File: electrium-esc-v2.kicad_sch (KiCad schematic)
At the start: 5 parts, among them J1 CAN

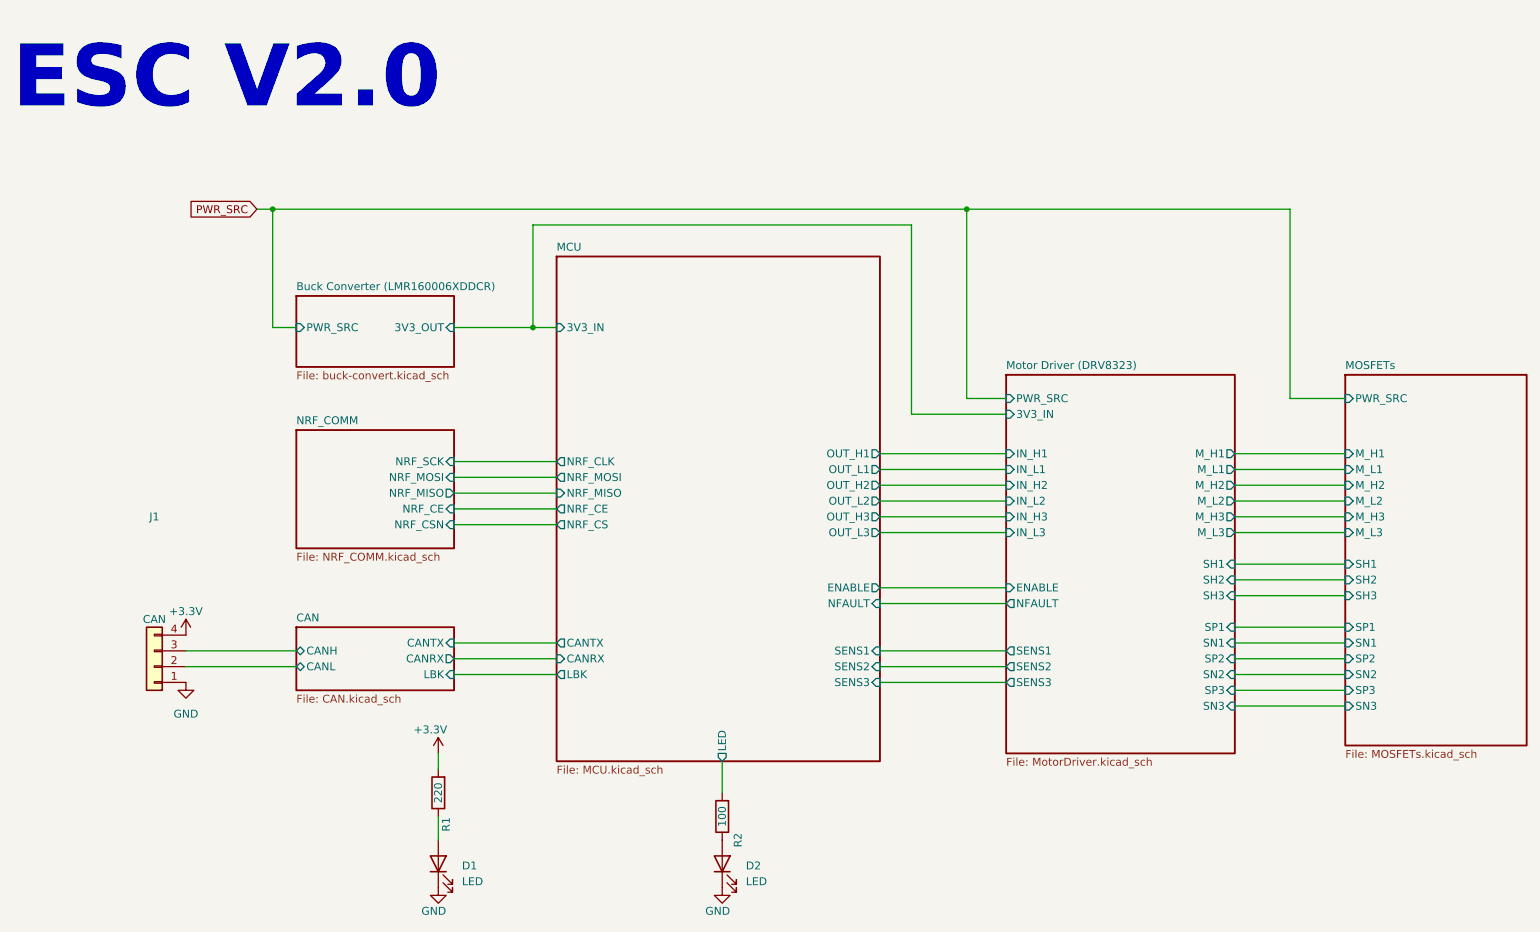
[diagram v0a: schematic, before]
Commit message: Add proper JST Connector
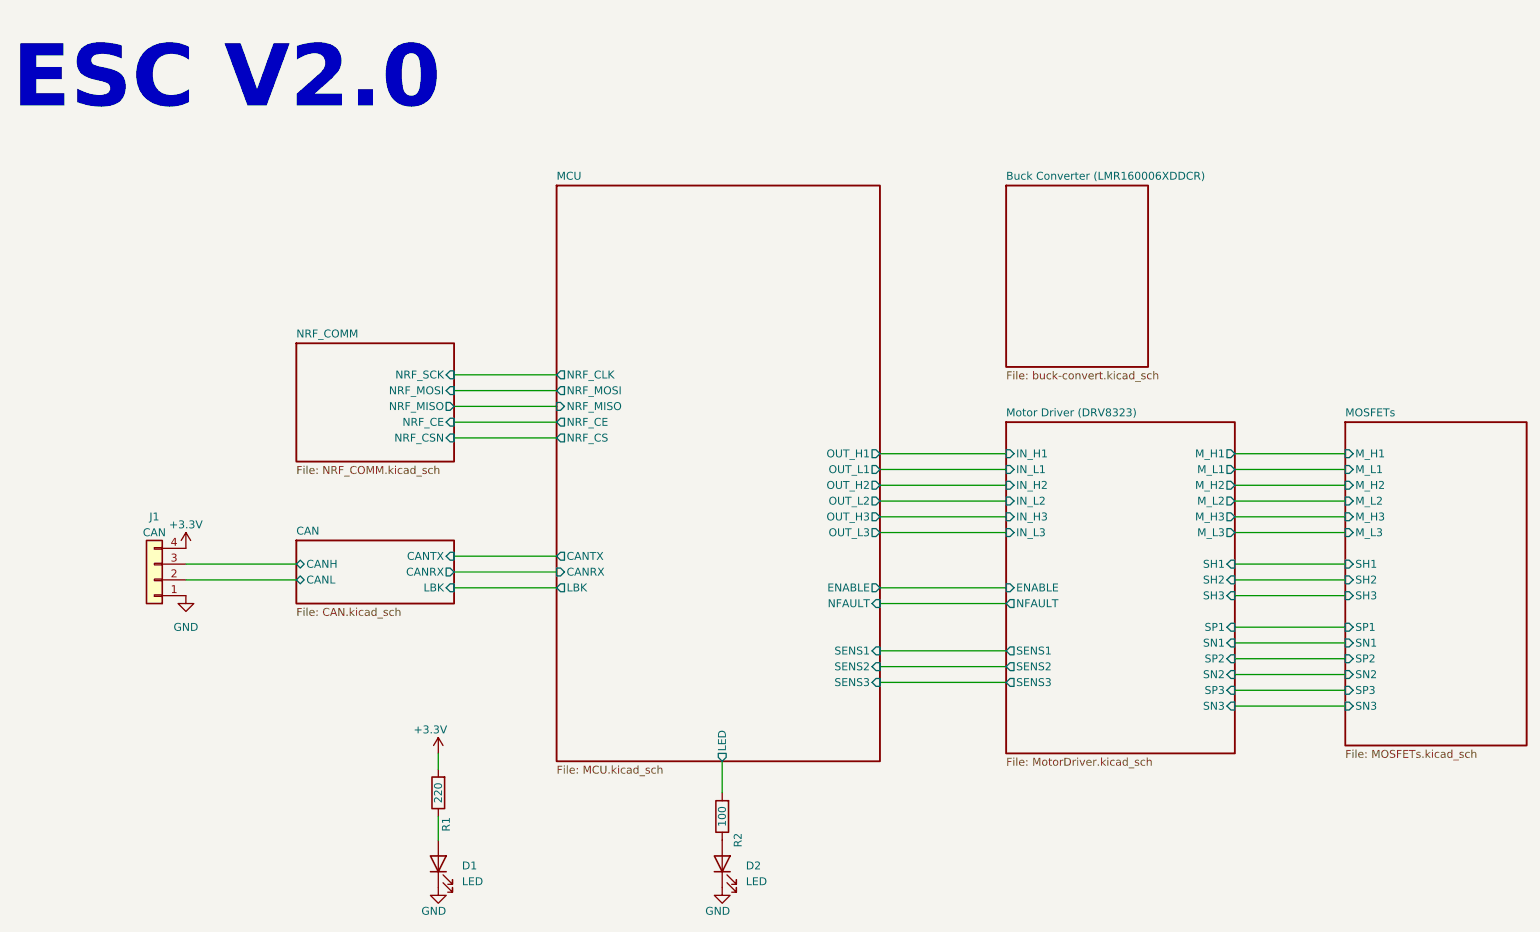
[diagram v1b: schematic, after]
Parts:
- J1: footprint (none) -> Connector_JST:JST_XH_B4B-XH-A_1x04_P2.50mm_Vertical
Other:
- sheet Buck Converter (LMR160006XDDCR) ports: added none; removed 3V3_OUT, PWR_SRC
- sheet MCU ports: added none; removed 3V3_IN
- sheet MOSFETs ports: added none; removed PWR_SRC
- sheet Motor Driver (DRV8323) ports: added none; removed 3V3_IN, PWR_SRC
- moved on the sheet: J1

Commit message: fix ERC
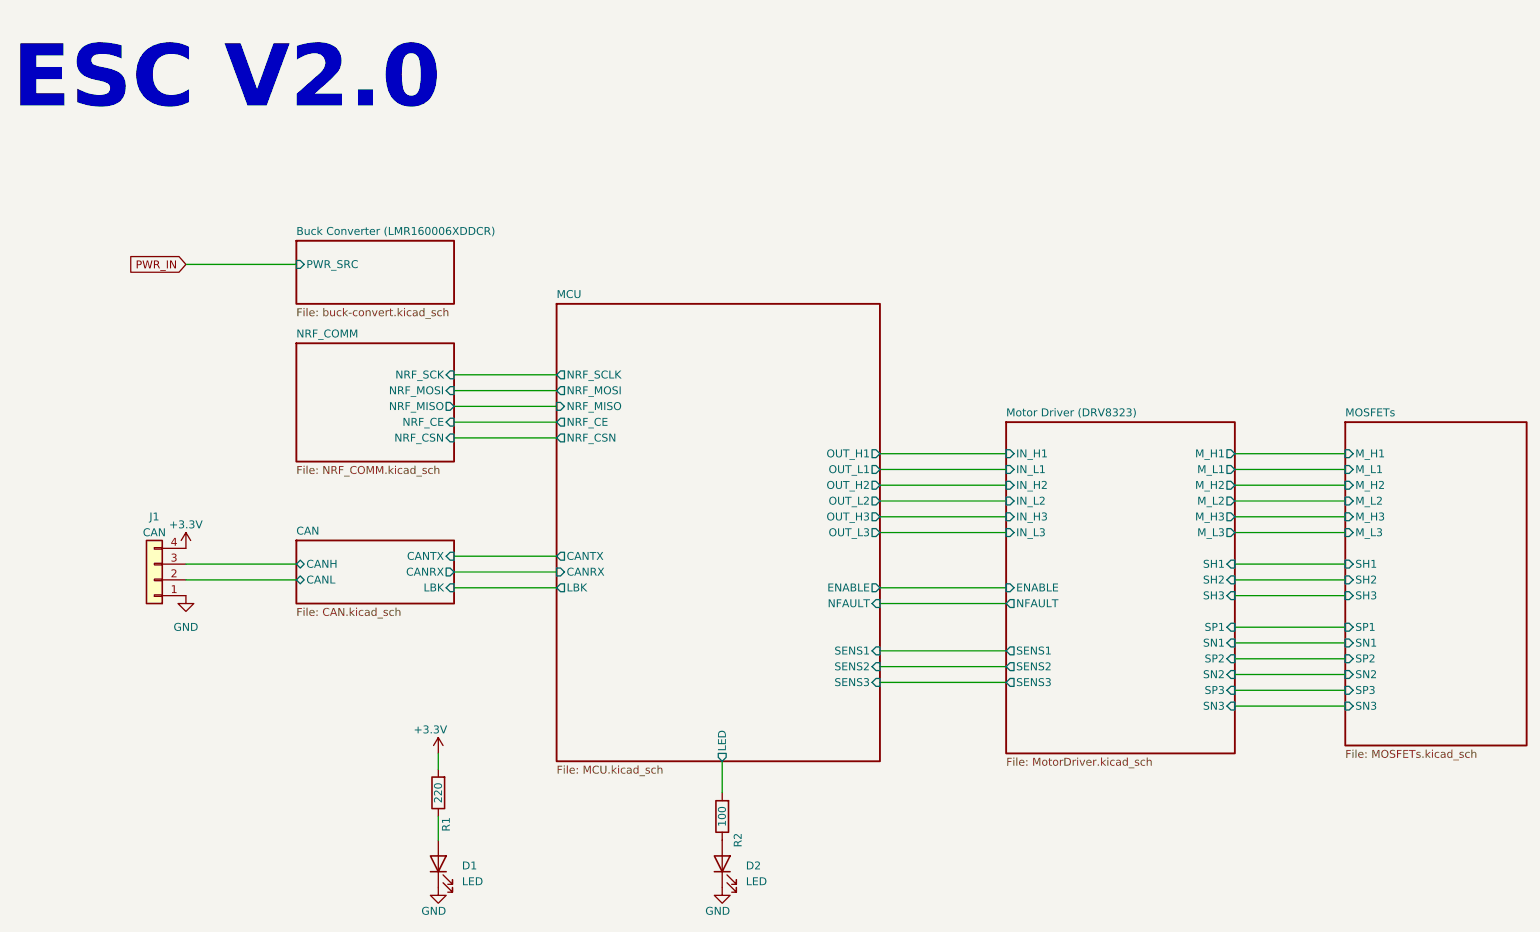
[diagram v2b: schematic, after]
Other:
- sheet Buck Converter (LMR160006XDDCR) ports: added PWR_SRC; removed none
- sheet MCU ports: added NRF_CSN, NRF_SCLK; removed NRF_CLK, NRF_CS
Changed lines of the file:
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@@
+    (stroke (width 0) (type default))
+  )
+  (wire (pts (xy 48.26 57.15) (xy 66.04 57.15))
     (stroke (width 0) (type default))
   )
@@
   (text "ESC V2.0" (at 20.32 33.02 0)
     (effects (font (size 10 10) (thickness 2) bold) (justify left bottom))
+  )
+  (global_label "PWR_IN" (shape input) (at 48.26 57.15 180) (fields_autoplaced)
+    (effects (font (size 1.27 1.27)) (justify right))
+    (property "Intersheetrefs" "${INTERSHEET_REFS}" (at 38.4599 57.15 0)
+      (effects (font (size 1.27 1.27)) (justify right) hide)
+    )
   )
   (symbol (lib_id "power:GND") (at 134.62 157.48 0) (unit 1)
@@
     )
   )
-  (sheet (at 107.95 44.45) (size 52.07 92.71) (fields_autoplaced)
+  (sheet (at 107.95 63.5) (size 52.07 73.66) (fields_autoplaced)
     (stroke (width 0.3) (type solid))
     (fill (color 0 0 0 0.0000))
-    (property "Sheetname" "MCU" (at 107.95 43.6646 0)
+    (property "Sheetname" "MCU" (at 107.95 62.7146 0)
       (effects (font (size 1.27 1.27)) (justify left bottom))
     )
@@
       (effects (font (size 1.27 1.27)) (justify left))
     )
-    (pin "NRF_CLK" output (at 107.95 74.93 180)
-      (effects (font (size 1.27 1.27)) (justify left))
-    )
-    (pin "NRF_CS" output (at 107.95 85.09 180)
+    (pin "NRF_SCLK" output (at 107.95 74.93 180)
+      (effects (font (size 1.27 1.27)) (justify left))
+    )
+    (pin "NRF_CSN" output (at 107.95 85.09 180)
       (effects (font (size 1.27 1.27)) (justify left))
     )
@@
     )
   )
-  (sheet (at 180.34 44.45) (size 22.86 29.21) (fields_autoplaced)
+  (sheet (at 66.04 53.34) (size 25.4 10.16) (fields_autoplaced)
     (stroke (width 0.3) (type solid))
     (fill (color 0 0 0 0.0000))
-    (property "Sheetname" "Buck Converter (LMR160006XDDCR)" (at 180.34 43.6646 0)
+    (property "Sheetname" "Buck Converter (LMR160006XDDCR)" (at 66.04 52.5546 0)
       (effects (font (size 1.27 1.27)) (justify left bottom))
     )
-    (property "Sheetfile" "buck-convert.kicad_sch" (at 180.34 74.3184 0)
+    (property "Sheetfile" "buck-convert.kicad_sch" (at 66.04 64.1584 0)
       (effects (font (size 1.27 1.27)) (justify left top))
     )
-    (instances
+    (pin "PWR_SRC" input (at 66.04 57.15 180)
+      (effects (font (size 1.27 1.27)) (justify left))
+    )
+    (instances

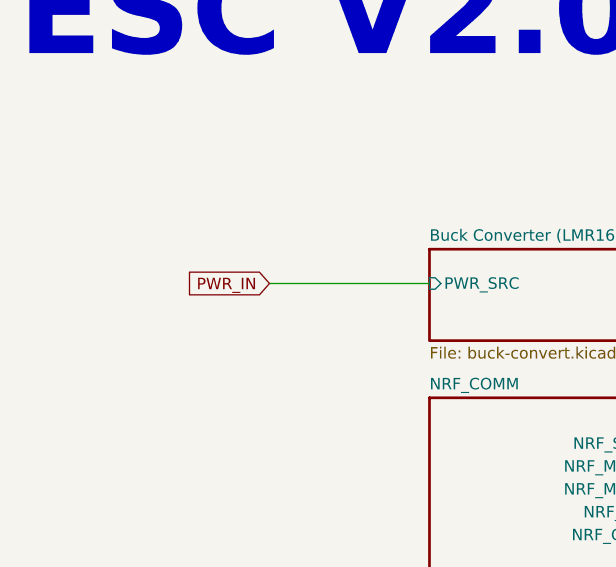
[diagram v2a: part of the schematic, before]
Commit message: Final schematic with no DRC errors
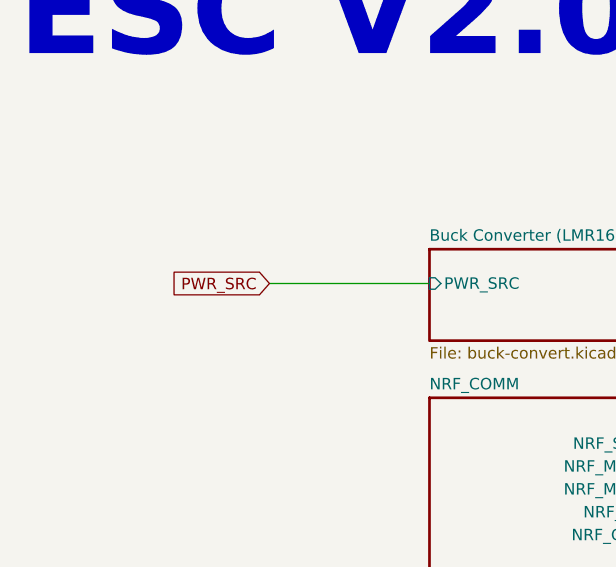
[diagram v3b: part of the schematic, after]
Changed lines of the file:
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@@
     (effects (font (size 10 10) (thickness 2) bold) (justify left bottom))
   )
-  (global_label "PWR_IN" (shape input) (at 48.26 57.15 180) (fields_autoplaced)
+  (global_label "PWR_SRC" (shape input) (at 48.26 57.15 180) (fields_autoplaced)
     (effects (font (size 1.27 1.27)) (justify right))
-    (property "Intersheetrefs" "${INTERSHEET_REFS}" (at 38.4599 57.15 0)
+    (property "Intersheetrefs" "${INTERSHEET_REFS}" (at 36.6457 57.15 0)
       (effects (font (size 1.27 1.27)) (justify right) hide)
     )
@@
       (effects (font (size 1.27 1.27)) (justify left))
     )
+    (pin "NRF_MOSI" output (at 107.95 77.47 180)
+      (effects (font (size 1.27 1.27)) (justify left))
+    )
+    (pin "NRF_MISO" input (at 107.95 80.01 180)
+      (effects (font (size 1.27 1.27)) (justify left))
+    )
+    (pin "OUT_L3" output (at 160.02 100.33 0)
+      (effects (font (size 1.27 1.27)) (justify right))
+    )
+    (pin "OUT_H3" output (at 160.02 97.79 0)
+      (effects (font (size 1.27 1.27)) (justify right))
+    )
+    (pin "OUT_L2" output (at 160.02 95.25 0)
+      (effects (font (size 1.27 1.27)) (justify right))
+    )
+    (pin "OUT_H2" output (at 160.02 92.71 0)
+      (effects (font (size 1.27 1.27)) (justify right))
+    )
+    (pin "OUT_L1" output (at 160.02 90.17 0)
+      (effects (font (size 1.27 1.27)) (justify right))
+    )
+    (pin "OUT_H1" output (at 160.02 87.63 0)
+      (effects (font (size 1.27 1.27)) (justify right))
+    )
+    (pin "ENABLE" output (at 160.02 109.22 0)
+      (effects (font (size 1.27 1.27)) (justify right))
+    )
+    (pin "NFAULT" input (at 160.02 111.76 0)
+      (effects (font (size 1.27 1.27)) (justify right))
+    )
+    (pin "SENS1" input (at 160.02 119.38 0)
+      (effects (font (size 1.27 1.27)) (justify right))
+    )
+    (pin "SENS2" input (at 160.02 121.92 0)
+      (effects (font (size 1.27 1.27)) (justify right))
+    )
+    (pin "SENS3" input (at 160.02 124.46 0)
+      (effects (font (size 1.27 1.27)) (justify right))
+    )
+    (pin "LED" output (at 134.62 137.16 270)
+      (effects (font (size 1.27 1.27)) (justify left))
+    )
+    (pin "CANTX" output (at 107.95 104.14 180)
+      (effects (font (size 1.27 1.27)) (justify left))
+    )
+    (pin "CANRX" input (at 107.95 106.68 180)
+      (effects (font (size 1.27 1.27)) (justify left))
+    )
+    (pin "LBK" output (at 107.95 109.22 180)
+      (effects (font (size 1.27 1.27)) (justify left))
+    )
     (pin "NRF_CSN" output (at 107.95 85.09 180)
       (effects (font (size 1.27 1.27)) (justify left))
     )
-    (pin "NRF_MOSI" output (at 107.95 77.47 180)
-      (effects (font (size 1.27 1.27)) (justify left))
-    )
-    (pin "NRF_MISO" input (at 107.95 80.01 180)
-      (effects (font (size 1.27 1.27)) (justify left))
-    )
-    (pin "OUT_L3" output (at 160.02 100.33 0)
-      (effects (font (size 1.27 1.27)) (justify right))
-    )
-    (pin "OUT_H3" output (at 160.02 97.79 0)
-      (effects (font (size 1.27 1.27)) (justify right))
-    )
-    (pin "OUT_L2" output (at 160.02 95.25 0)
-      (effects (font (size 1.27 1.27)) (justify right))
-    )
-    (pin "OUT_H2" output (at 160.02 92.71 0)
-      (effects (font (size 1.27 1.27)) (justify right))
-    )
-    (pin "OUT_L1" output (at 160.02 90.17 0)
-      (effects (font (size 1.27 1.27)) (justify right))
-    )
-    (pin "OUT_H1" output (at 160.02 87.63 0)
-      (effects (font (size 1.27 1.27)) (justify right))
-    )
-    (pin "ENABLE" output (at 160.02 109.22 0)
-      (effects (font (size 1.27 1.27)) (justify right))
-    )
-    (pin "NFAULT" input (at 160.02 111.76 0)
-      (effects (font (size 1.27 1.27)) (justify right))
-    )
-    (pin "SENS1" input (at 160.02 119.38 0)
-      (effects (font (size 1.27 1.27)) (justify right))
-    )
-    (pin "SENS2" input (at 160.02 121.92 0)
-      (effects (font (size 1.27 1.27)) (justify right))
-    )
-    (pin "SENS3" input (at 160.02 124.46 0)
-      (effects (font (size 1.27 1.27)) (justify right))
-    )
-    (pin "LED" output (at 134.62 137.16 270)
-      (effects (font (size 1.27 1.27)) (justify left))
-    )
-    (pin "CANTX" output (at 107.95 104.14 180)
-      (effects (font (size 1.27 1.27)) (justify left))
-    )
-    (pin "CANRX" input (at 107.95 106.68 180)
-      (effects (font (size 1.27 1.27)) (justify left))
-    )
-    (pin "LBK" output (at 107.95 109.22 180)
-      (effects (font (size 1.27 1.27)) (justify left))
-    )
